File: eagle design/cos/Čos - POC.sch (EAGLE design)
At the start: 113 parts, among them IC1 SQJ952EP-T1_GE3, IC10 LM74670QDGKRQ1, IC11 LM74670QDGKRQ1, IC12 LM74670QDGKRQ1, IC13 MCP73871-2CCI/ML, IC14 MCP2515, IC15 LM74670QDGKRQ1, IC16 LM74670QDGKRQ1, IC17 MCP23S08-E/ML, IC18 MCP2561-2, IC19 AD5160BRJZ5-R2, IC2 SQJ952EP-T1_GE3, IC20 MP3221GJ-P, IC21 SQJ952EP-T1_GE3, IC22 LM74670QDGKRQ1, IC23 SQJ952EP-T1_GE3, IC3 LM74670QDGKRQ1, IC4 SQJ952EP-T1_GE3, IC5 FDMQ8403, IC6 TPS630702RNMT, IC7 LMP92064SD/NOPB, IC8 ATTINY4313-MMH, IC9 PBRC8.00GR50X000

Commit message: - minor corrections to brd, ERC&DRC are fine - added constructors for cos' devices
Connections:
- net COMP_IN renamed COMPARATOR_IN
- net PS/SYNC renamed TPS630702_PWM
- removed net AD5160_CS: IC17.15_GP6, IC19.6_!CS!, R19.8
- removed net LMP92064SD_CS: IC17.16_GP7, IC7.CSB_14, R19.6
- removed net N$6: IC8.PCINT16/OC0B/T1-PD5
- new net SPI_SS_AD5160: IC19.6_!CS!, IC8.PCINT16/OC0B/T1-PD5, R19.8
- new net SPI_SS_LMP92064SD: IC7.CSB_14, IC8.PCINT17/ICPI-PD6, R19.6
- net INT_MCP23S08: now also IC8.PCINT15/T0-PD4
- net N$2: now also IC17.15_GP6; no longer IC8.PCINT15/T0-PD4
- net N$7: now also IC17.16_GP7; no longer IC8.PCINT17/ICPI-PD6

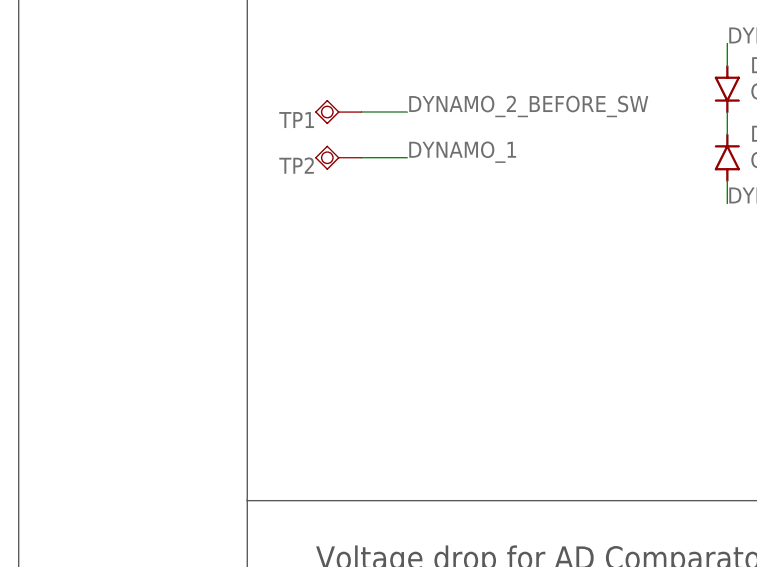
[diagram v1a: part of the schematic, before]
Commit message: - minor routing changes - added fiducials
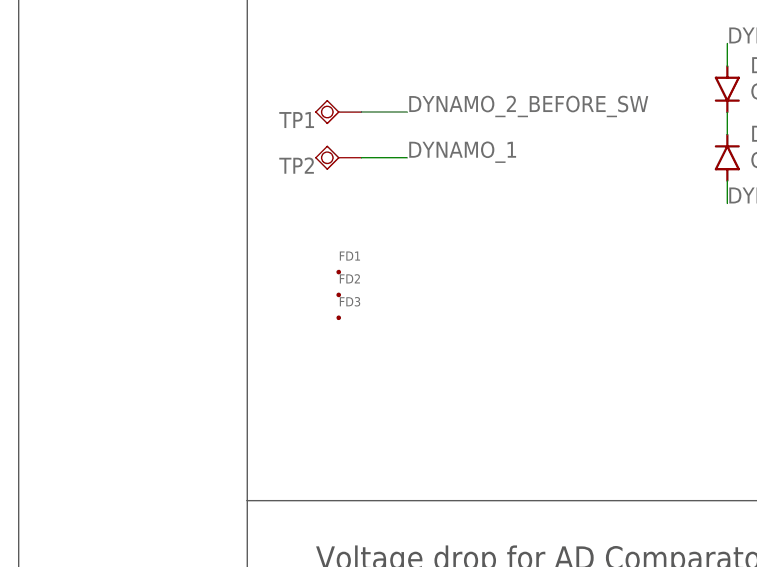
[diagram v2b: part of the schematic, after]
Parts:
- added FD1, FD2, FD3: FID_40MIL, Fiducial:FID_40MIL
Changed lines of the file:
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@@
 <?xml version="1.0" encoding="utf-8"?>
 <!DOCTYPE eagle SYSTEM "eagle.dtd">
-<eagle version="9.4.2">
+<eagle version="9.4.0">
 <drawing>
 <settings>
@@
 <part name="TP7_OUT" library="testpad" library_urn="urn:adsk.eagle:library:385" deviceset="PTR1" device="TP10SQ" package3d_urn="urn:adsk.eagle:package:27962/1"/>
 <part name="IC20" library="MP3221–2.7A, 1.2MHZ, HIGH-EFFICIENCY STEP UP CONVERTER WITH INPUT DISCONNECT" deviceset="MP3221" device="" value="MP3221GJ-P"/>
+<part name="FD1" library="Fiducial" deviceset="FID" device="_40MIL"/>
+<part name="FD2" library="Fiducial" deviceset="FID" device="_40MIL"/>
+<part name="FD3" library="Fiducial" deviceset="FID" device="_40MIL"/>
 </parts>
 <sheets>
@@
 <attribute name="VALUE" x="393.7" y="116.84" size="1.27" layer="96" font="vector" align="center"/>
 </instance>
+<instance part="FD1" gate="G$2" x="-25.4" y="1031.24" smashed="yes">
+<attribute name="NAME" x="-25.4" y="1032.51" size="1.016" layer="95" font="vector" ratio="12"/>
+</instance>
+<instance part="FD2" gate="G$2" x="-25.4" y="1028.7" smashed="yes">
+<attribute name="NAME" x="-25.4" y="1029.97" size="1.016" layer="95" font="vector" ratio="12"/>
+</instance>
+<instance part="FD3" gate="G$2" x="-25.4" y="1026.16" smashed="yes">
+<attribute name="NAME" x="-25.4" y="1027.43" size="1.016" layer="95" font="vector" ratio="12"/>
+</instance>
 </instances>

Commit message: - specified resistor divider for LMP92064SD
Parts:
- R7: value 100k -> 320k; device rcl:R-EU_R1206 -> rcl:R-EU_R0402
- R8: device rcl:R-EU_R1206 -> rcl:R-EU_R0402
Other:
- note added: "Full Scale Input Voltage = 2.048V 8.5V are set to be 2.024V on INVP via the resistor divider"
- note removed: "Full Scale Input Voltage = 2.048V"
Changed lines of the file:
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@@
 <?xml version="1.0" encoding="utf-8"?>
 <!DOCTYPE eagle SYSTEM "eagle.dtd">
-<eagle version="9.4.0">
+<eagle version="9.4.2">
 <drawing>
 <settings>
@@
 <grid distance="0.1" unitdist="inch" unit="inch" style="lines" multiple="1" display="no" altdistance="0.01" altunitdist="inch" altunit="inch"/>
 <layers>
-<layer number="1" name="Top" color="4" fill="1" visible="no" active="no"/>
-<layer number="2" name="Route2" color="26" fill="1" visible="no" active="no"/>
-<layer number="3" name="Route3" color="4" fill="3" visible="no" active="no"/>
-<layer number="4" name="Route4" color="1" fill="4" visible="no" active="no"/>
-<layer number="5" name="Route5" color="4" fill="4" visible="no" active="no"/>
-<layer number="6" name="Route6" color="1" fill="8" visible="no" active="no"/>
-<layer number="7" name="Route7" color="4" fill="8" visible="no" active="no"/>
-<layer number="8" name="Route8" color="1" fill="2" visible="no" active="no"/>
-<layer number="9" name="Route9" color="4" fill="2" visible="no" active="no"/>
-<layer number="10" name="Route10" color="1" fill="7" visible="no" active="no"/>
-<layer number="11" name="Route11" color="4" fill="7" visible="no" active="no"/>
-<layer number="12" name="Route12" color="1" fill="5" visible="no" active="no"/>
-<layer number="13" name="Route13" color="4" fill="5" visible="no" active="no"/>
-<layer number="14" name="Route14" color="1" fill="6" visible="no" active="no"/>
-<layer number="15" name="Route15" color="24" fill="1" visible="no" active="no"/>
-<layer number="16" name="Bottom" color="1" fill="1" visible="no" active="no"/>
-<layer number="17" name="Pads" color="2" fill="1" visible="no" active="no"/>
-<layer number="18" name="Vias" color="2" fill="1" visible="no" active="no"/>
-<layer number="19" name="Unrouted" color="6" fill="1" visible="no" active="no"/>
-<layer number="20" name="Dimension" color="24" fill="1" visible="no" active="no"/>
-<layer number="21" name="tPlace" color="7" fill="1" visible="no" active="no"/>
-<layer number="22" name="bPlace" color="7" fill="1" visible="no" active="no"/>
-<layer number="23" name="tOrigins" color="15" fill="1" visible="no" active="no"/>
-<layer number="24" name="bOrigins" color="15" fill="1" visible="no" active="no"/>
-<layer number="25" name="tNames" color="7" fill="1" visible="no" active="no"/>
-<layer number="26" name="bNames" color="7" fill="1" visible="no" active="no"/>
-<layer number="27" name="tValues" color="7" fill="1" visible="no" active="no"/>
-<layer number="28" name="bValues" color="7" fill="1" visible="no" active="no"/>
+<layer number="1" name="Top" color="4" fill="1" visible="yes" active="no"/>
+<layer number="2" name="Route2" color="26" fill="1" visible="yes" active="no"/>
+<layer number="3" name="Route3" color="4" fill="3" visible="yes" active="no"/>
+<layer number="4" name="Route4" color="1" fill="4" visible="yes" active="no"/>
+<layer number="5" name="Route5" color="4" fill="4" visible="yes" active="no"/>
+<layer number="6" name="Route6" color="1" fill="8" visible="yes" active="no"/>
+<layer number="7" name="Route7" color="4" fill="8" visible="yes" active="no"/>
+<layer number="8" name="Route8" color="1" fill="2" visible="yes" active="no"/>
+<layer number="9" name="Route9" color="4" fill="2" visible="yes" active="no"/>
+<layer number="10" name="Route10" color="1" fill="7" visible="yes" active="no"/>
+<layer number="11" name="Route11" color="4" fill="7" visible="yes" active="no"/>
+<layer number="12" name="Route12" color="1" fill="5" visible="yes" active="no"/>
+<layer number="13" name="Route13" color="4" fill="5" visible="yes" active="no"/>
+<layer number="14" name="Route14" color="1" fill="6" visible="yes" active="no"/>
+<layer number="15" name="Route15" color="24" fill="1" visible="yes" active="no"/>
+<layer number="16" name="Bottom" color="1" fill="1" visible="yes" active="no"/>
+<layer number="17" name="Pads" color="2" fill="1" visible="yes" active="no"/>
+<layer number="18" name="Vias" color="2" fill="1" visible="yes" active="no"/>
+<layer number="19" name="Unrouted" color="6" fill="1" visible="yes" active="no"/>
+<layer number="20" name="Dimension" color="24" fill="1" visible="yes" active="no"/>
+<layer number="21" name="tPlace" color="7" fill="1" visible="yes" active="no"/>
+<layer number="22" name="bPlace" color="7" fill="1" visible="yes" active="no"/>
+<layer number="23" name="tOrigins" color="15" fill="1" visible="yes" active="no"/>
+<layer number="24" name="bOrigins" color="15" fill="1" visible="yes" active="no"/>
+<layer number="25" name="tNames" color="7" fill="1" visible="yes" active="no"/>
+<layer number="26" name="bNames" color="7" fill="1" visible="yes" active="no"/>
+<layer number="27" name="tValues" color="7" fill="1" visible="yes" active="no"/>
+<layer number="28" name="bValues" color="7" fill="1" visible="yes" active="no"/>
 <layer number="29" name="tStop" color="7" fill="3" visible="no" active="no"/>
 <layer number="30" name="bStop" color="7" fill="6" visible="no" active="no"/>
@@
 <layer number="35" name="tGlue" color="7" fill="4" visible="no" active="no"/>
 <layer number="36" name="bGlue" color="7" fill="5" visible="no" active="no"/>
-<layer number="37" name="tTest" color="7" fill="1" visible="no" active="no"/>
-<layer number="38" name="bTest" color="7" fill="1" visible="no" active="no"/>
+<layer number="37" name="tTest" color="7" fill="1" visible="yes" active="no"/>
+<layer number="38" name="bTest" color="7" fill="1" visible="yes" active="no"/>
 <layer number="39" name="tKeepout" color="4" fill="11" visible="no" active="no"/>
 <layer number="40" name="bKeepout" color="1" fill="11" visible="no" active="no"/>
@@
 <layer number="44" name="Drills" color="7" fill="1" visible="no" active="no"/>
 <layer number="45" name="Holes" color="7" fill="1" visible="no" active="no"/>
-<layer number="46" name="Milling" color="3" fill="1" visible="no" active="no"/>
-<layer number="47" name="Measures" color="7" fill="1" visible="no" active="no"/>
-<layer number="48" name="Document" color="7" fill="1" visible="no" active="no"/>
-<layer number="49" name="Reference" color="7" fill="1" visible="no" active="no"/>
-<layer number="50" name="dxf" color="7" fill="1" visible="no" active="no"/>
-<layer number="51" name="tDocu" color="7" fill="1" visible="no" active="no"/>
-<layer number="52" name="bDocu" color="7" fill="1" visible="no" active="no"/>
-<layer number="53" name="tGND_GNDA" color="7" fill="9" visible="no" active="no"/>
-<layer number="54" name="bGND_GNDA" color="1" fill="9" visible="no" active="no"/>
-<layer number="56" name="wert" color="7" fill="1" visible="no" active="no"/>
-<layer number="57" name="tCAD" color="7" fill="1" visible="no" active="no"/>
-<layer number="59" name="tCarbon" color="7" fill="1" visible="no" active="no"/>
-<layer number="60" name="bCarbon" color="7" fill="1" visible="no" active="no"/>
+<layer number="46" name="Milling" color="3" fill="1" visible="yes" active="no"/>
+<layer number="47" name="Measures" color="7" fill="1" visible="yes" active="no"/>
+<layer number="48" name="Document" color="7" fill="1" visible="yes" active="no"/>
+<layer number="49" name="Reference" color="7" fill="1" visible="yes" active="no"/>
+<layer number="50" name="dxf" color="7" fill="1" visible="yes" active="no"/>
+<layer number="51" name="tDocu" color="7" fill="1" visible="yes" active="no"/>
+<layer number="52" name="bDocu" color="7" fill="1" visible="yes" active="no"/>
+<layer number="53" name="tGND_GNDA" color="7" fill="9" visible="yes" active="no"/>
+<layer number="54" name="bGND_GNDA" color="1" fill="9" visible="yes" active="no"/>
+<layer number="56" name="wert" color="7" fill="1" visible="yes" active="no"/>
+<layer number="57" name="tCAD" color="7" fill="1" visible="yes" active="no"/>
+<layer number="59" name="tCarbon" color="7" fill="1" visible="yes" active="no"/>
+<layer number="60" name="bCarbon" color="7" fill="1" visible="yes" active="no"/>
 <layer number="88" name="SimResults" color="9" fill="1" visible="yes" active="yes"/>
 <layer number="89" name="SimProbes" color="9" fill="1" visible="yes" active="yes"/>
@@
 <part name="IC7" library="LMP92064SD - LMP92064 Precision Low-Side, 125-kSps Simultaneous Sampling Current Sensor and Voltage Monitor With SPI" deviceset="LMP92064SD" device="" value="LMP92064SD/NOPB"/>
 <part name="R2" library="rcl" library_urn="urn:adsk.eagle:library:334" deviceset="R-EU_" device="R1206" package3d_urn="urn:adsk.eagle:package:23540/2" value="100k"/>
-<part name="R7" library="rcl" library_urn="urn:adsk.eagle:library:334" deviceset="R-EU_" device="R1206" package3d_urn="urn:adsk.eagle:package:23540/2" value="100k"/>
-<part name="R8" library="rcl" library_urn="urn:adsk.eagle:library:334" deviceset="R-EU_" device="R1206" package3d_urn="urn:adsk.eagle:package:23540/2" value="100k"/>
+<part name="R7" library="rcl" library_urn="urn:adsk.eagle:library:334" deviceset="R-EU_" device="R0402" package3d_urn="urn:adsk.eagle:package:23547/3" value="320k"/>
+<part name="R8" library="rcl" library_urn="urn:adsk.eagle:library:334" deviceset="R-EU_" device="R0402" package3d_urn="urn:adsk.eagle:package:23547/3" value="100k"/>
 <part name="C14" library="rcl" library_urn="urn:adsk.eagle:library:334" deviceset="C-EU" device="C0402" package3d_urn="urn:adsk.eagle:package:23626/2" value="0.1μF"/>
 <part name="C12" library="rcl" library_urn="urn:adsk.eagle:library:334" deviceset="C-EU" device="C0402" package3d_urn="urn:adsk.eagle:package:23626/2" value="0.1μF"/>
@@
 <text x="208.28" y="508" size="6.4516" layer="94">TP4</text>
 <text x="447.04" y="132.08" size="6.4516" layer="94">TP6</text>
-<text x="38.1" y="403.86" size="1.778" layer="97">Full Scale Input Voltage = 2.048V</text>
+<text x="38.1" y="403.86" size="1.778" layer="97">Full Scale Input Voltage = 2.048V
+8.5V are set to be 2.024V on INVP
+via the resistor divider</text>
 <text x="106.68" y="330.2" size="1.778" layer="97">maximum operatin current Imax=15mA</text>
 <text x="-33.02" y="365.76" size="1.778" layer="97">Rsense</text>

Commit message: specified resistor for current sense
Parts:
- added R28: 741X083331JP / 330Ω, 741X083331JP Resistor Array:741X083331JP
- R2: value 100k -> 43mR, 200mW; device rcl:R-EU_R1206 -> rcl:R-EU_R2512
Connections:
- removed net N$2: IC17.15_GP6
- new net N$10: IC17.13_GP4, R28.3
- new net N$11: IC17.12_GP3, R28.1
- new net N$6: IC17.14_GP5, R28.5
- net GATE_DELON: now also R28.6; no longer IC17.14_GP5
- net GATE_GRAETZ: now also R28.2; no longer IC17.12_GP3
- net GATE_TUNING-CAP: now also R28.4; no longer IC17.13_GP4
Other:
- note added: "Imax = 2A current sense fill scale range: 81.92mV Rsense = 0.08192V / 2A = 40.96 mOhm"
- moved on the sheet: C11, C12, C13, C14, C9, IC7, R2, R7, R8, TP7_IN, TP7_OUT
